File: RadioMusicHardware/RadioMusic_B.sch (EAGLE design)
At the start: 32 parts, among them IC4 TL074, U1 TEENSY_3.1_TW

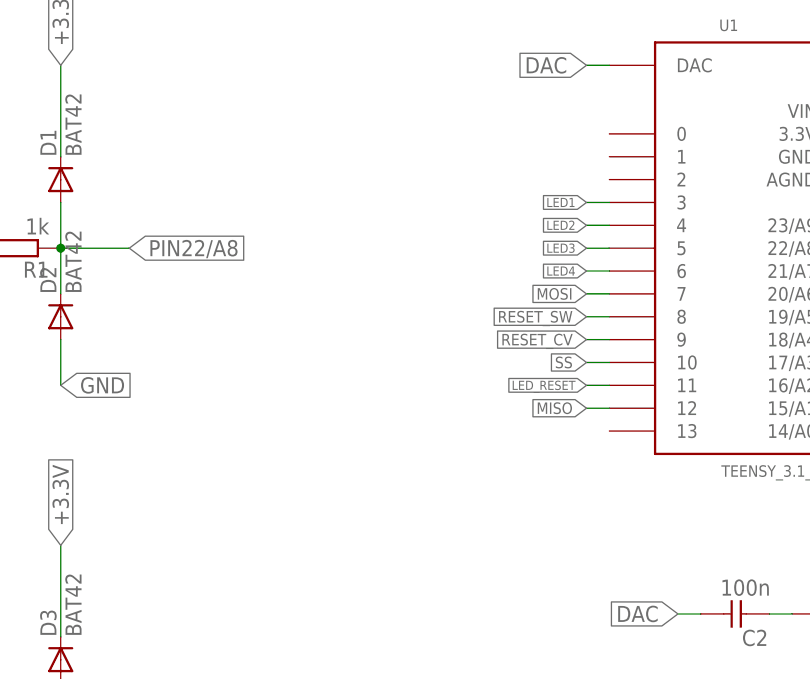
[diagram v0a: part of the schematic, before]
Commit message: Layout experiments - back board output not completed
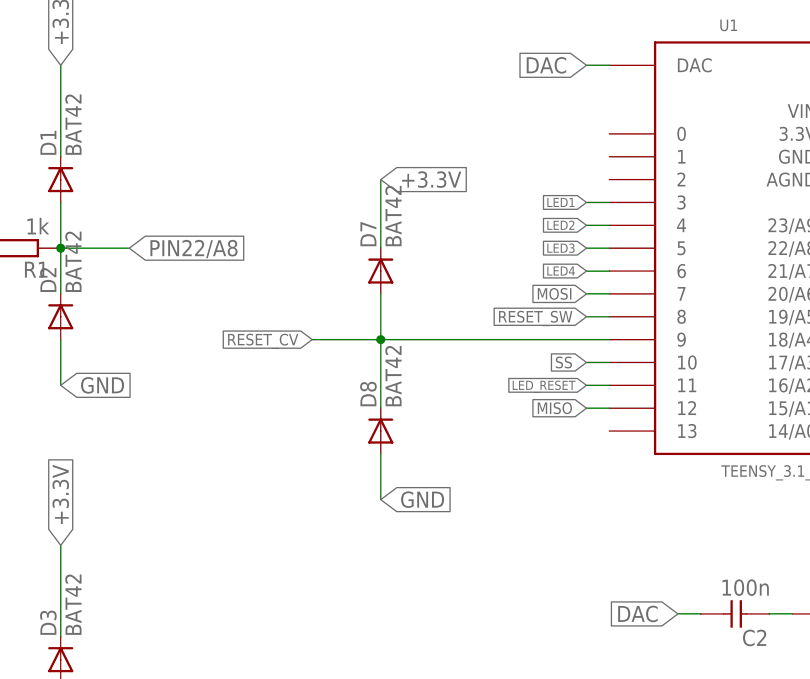
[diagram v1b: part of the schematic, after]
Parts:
- added D7, D8: BAT42, MusicThingModular:SMALL_DIODEDO35-7
- D1, D2, D3, D4: device diode:BAT81 -> MusicThingModular:SMALL_DIODEDO35-7
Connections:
- net +3.3V: now also D7.C
- net GND: now also D8.A
- net RESET_CV: now also D7.A, D8.C
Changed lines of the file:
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@@
 <part name="SUPPLY2" library="supply2" deviceset="GND" device=""/>
 <part name="U1" library="TomW" deviceset="TEENSY_3.1_TW" device=""/>
-<part name="D1" library="diode" deviceset="BAT81" device="" value="BAT42"/>
-<part name="D2" library="diode" deviceset="BAT81" device="" value="BAT42"/>
+<part name="D1" library="MusicThingModular" deviceset="SMALL_DIODE" device="DO35-7" value="BAT42"/>
+<part name="D2" library="MusicThingModular" deviceset="SMALL_DIODE" device="DO35-7" value="BAT42"/>
 <part name="R4" library="MusicThingModular" deviceset="RESISTOR" device="7MM" value="8.2k"/>
 <part name="R3" library="MusicThingModular" deviceset="RESISTOR" device="7MM" value="8.2k"/>
@@
 <part name="C2" library="TomW" deviceset="C-EU" device="050-025X075" value="100n"/>
 <part name="R1" library="TomW" deviceset="R-EU_" device="STANDARD_RESISTOR" value="1k"/>
-<part name="D3" library="diode" deviceset="BAT81" device="" value="BAT42"/>
-<part name="D4" library="diode" deviceset="BAT81" device="" value="BAT42"/>
+<part name="D3" library="MusicThingModular" deviceset="SMALL_DIODE" device="DO35-7" value="BAT42"/>
+<part name="D4" library="MusicThingModular" deviceset="SMALL_DIODE" device="DO35-7" value="BAT42"/>
 <part name="R2" library="TomW" deviceset="R-EU_" device="STANDARD_RESISTOR" value="1k"/>
 <part name="L1" library="inductors" deviceset="BL0" device="1RN1A"/>
@@
 <part name="IC1" library="v-reg" deviceset="78LXX" device=""/>
 <part name="R6" library="MusicThingModular" deviceset="RESISTOR" device="7MM" value="100k"/>
+<part name="D7" library="MusicThingModular" deviceset="SMALL_DIODE" device="DO35-7" value="BAT42"/>
+<part name="D8" library="MusicThingModular" deviceset="SMALL_DIODE" device="DO35-7" value="BAT42"/>
 </parts>
 <sheets>
@@
 <instance part="IC4" gate="D" x="182.88" y="71.12"/>
 <instance part="IC4" gate="A" x="231.14" y="68.58"/>
-<instance part="D1" gate="1" x="40.64" y="121.92" rot="R90"/>
-<instance part="D2" gate="1" x="40.64" y="106.68" rot="R90"/>
+<instance part="D1" gate="G$1" x="40.64" y="121.92" rot="R90"/>
+<instance part="D2" gate="G$1" x="40.64" y="106.68" rot="R90"/>
 <instance part="R4" gate="G$1" x="149.86" y="73.66"/>
 <instance part="R3" gate="G$1" x="127" y="73.66" rot="R180"/>
@@
 <instance part="R1" gate="G$1" x="35.56" y="114.3" rot="R180"/>
 <instance part="IC4" gate="C" x="17.78" y="60.96"/>
-<instance part="D3" gate="1" x="40.64" y="68.58" rot="R90"/>
-<instance part="D4" gate="1" x="40.64" y="53.34" rot="R90"/>
+<instance part="D3" gate="G$1" x="40.64" y="68.58" rot="R90"/>
+<instance part="D4" gate="G$1" x="40.64" y="53.34" rot="R90"/>
 <instance part="R2" gate="G$1" x="35.56" y="60.96" rot="R180"/>
 <instance part="L1" gate="G$1" x="149.86" y="33.02" rot="R180"/>
@@
 <instance part="IC1" gate="1" x="91.44" y="38.1"/>
 <instance part="R6" gate="G$1" x="162.56" y="55.88" rot="R90"/>
+<instance part="D7" gate="G$1" x="76.2" y="111.76" rot="R90"/>
+<instance part="D8" gate="G$1" x="76.2" y="93.98" rot="R90"/>
 </instances>
 <busses>
@@
 </segment>
 <segment>
-<pinref part="D2" gate="1" pin="A"/>
+<pinref part="D2" gate="G$1" pin="A"/>
 <wire x1="40.64" y1="99.06" x2="40.64" y2="104.14" width="0.1524" layer="91"/>
 <label x="40.64" y="99.06" size="1.778" layer="95" xref="yes"/>
 </segment>
 <segment>
-<pinref part="D4" gate="1" pin="A"/>
+<pinref part="D4" gate="G$1" pin="A"/>
 <wire x1="40.64" y1="45.72" x2="40.64" y2="50.8" width="0.1524" layer="91"/>
 <label x="40.64" y="45.72" size="1.778" layer="95" xref="yes"/>
+</segment>
+<segment>
+<pinref part="D8" gate="G$1" pin="A"/>
+<wire x1="76.2" y1="91.44" x2="76.2" y2="86.36" width="0.1524" layer="91"/>
+<label x="76.2" y="86.36" size="1.778" layer="95" xref="yes"/>
 </segment>
 </net>
@@
 </segment>
 <segment>
-<pinref part="D1" gate="1" pin="C"/>
+<pinref part="D1" gate="G$1" pin="C"/>
 <wire x1="40.64" y1="134.62" x2="40.64" y2="124.46" width="0.1524" layer="91"/>
 <label x="40.64" y="134.62" size="1.778" layer="95" rot="R90" xref="yes"/>
 </segment>
 <segment>
-<pinref part="D3" gate="1" pin="C"/>
+<pinref part="D3" gate="G$1" pin="C"/>
 <wire x1="40.64" y1="81.28" x2="40.64" y2="71.12" width="0.1524" layer="91"/>
 <label x="40.64" y="81.28" size="1.778" layer="95" rot="R90" xref="yes"/>
@@
 <label x="195.58" y="109.22" size="1.016" layer="95" rot="R180" xref="yes"/>
 </segment>
+<segment>
+<pinref part="D7" gate="G$1" pin="C"/>
+<wire x1="76.2" y1="114.3" x2="76.2" y2="121.92" width="0.1524" layer="91"/>
+<label x="76.2" y="121.92" size="1.778" layer="95" xref="yes"/>
+</segment>
 </net>
 <net name="CHANNEL_CV" class="0">
@@
 </segment>
 <segment>
-<pinref part="D1" gate="1" pin="A"/>
+<pinref part="D1" gate="G$1" pin="A"/>
 <wire x1="40.64" y1="119.38" x2="40.64" y2="114.3" width="0.1524" layer="91"/>
-<pinref part="D2" gate="1" pin="C"/>
+<pinref part="D2" gate="G$1" pin="C"/>
 <wire x1="40.64" y1="109.22" x2="40.64" y2="114.3" width="0.1524" layer="91"/>
 <junction x="40.64" y="114.3"/>
@@
 <net name="PIN20/A6" class="0">
 <segment>
-<pinref part="D3" gate="1" pin="A"/>
+<pinref part="D3" gate="G$1" pin="A"/>
 <wire x1="40.64" y1="66.04" x2="40.64" y2="60.96" width="0.1524" layer="91"/>
-<pinref part="D4" gate="1" pin="C"/>
+<pinref part="D4" gate="G$1" pin="C"/>
 <wire x1="40.64" y1="55.88" x2="40.64" y2="60.96" width="0.1524" layer="91"/>
 <junction x="40.64" y="60.96"/>
@@
 <segment>
 <pinref part="U1" gate="G$1" pin="9"/>
-<wire x1="99.06" y1="104.14" x2="101.6" y2="104.14" width="0.1524" layer="91"/>
-<label x="99.06" y="104.14" size="1.27" layer="95" rot="R180" xref="yes"/>
-</segment>
-<segment>
+<wire x1="68.58" y1="104.14" x2="76.2" y2="104.14" width="0.1524" layer="91"/>
+<label x="68.58" y="104.14" size="1.27" layer="95" rot="R180" xref="yes"/>
+<pinref part="D7" gate="G$1" pin="A"/>
+<wire x1="76.2" y1="104.14" x2="101.6" y2="104.14" width="0.1524" layer="91"/>
+<wire x1="76.2" y1="109.22" x2="76.2" y2="104.14" width="0.1524" layer="91"/>
+<junction x="76.2" y="104.14"/>
+<pinref part="D8" gate="G$1" pin="C"/>
+<wire x1="76.2" y1="96.52" x2="76.2" y2="104.14" width="0.1524" layer="91"/>
+</segment>
+<segment>

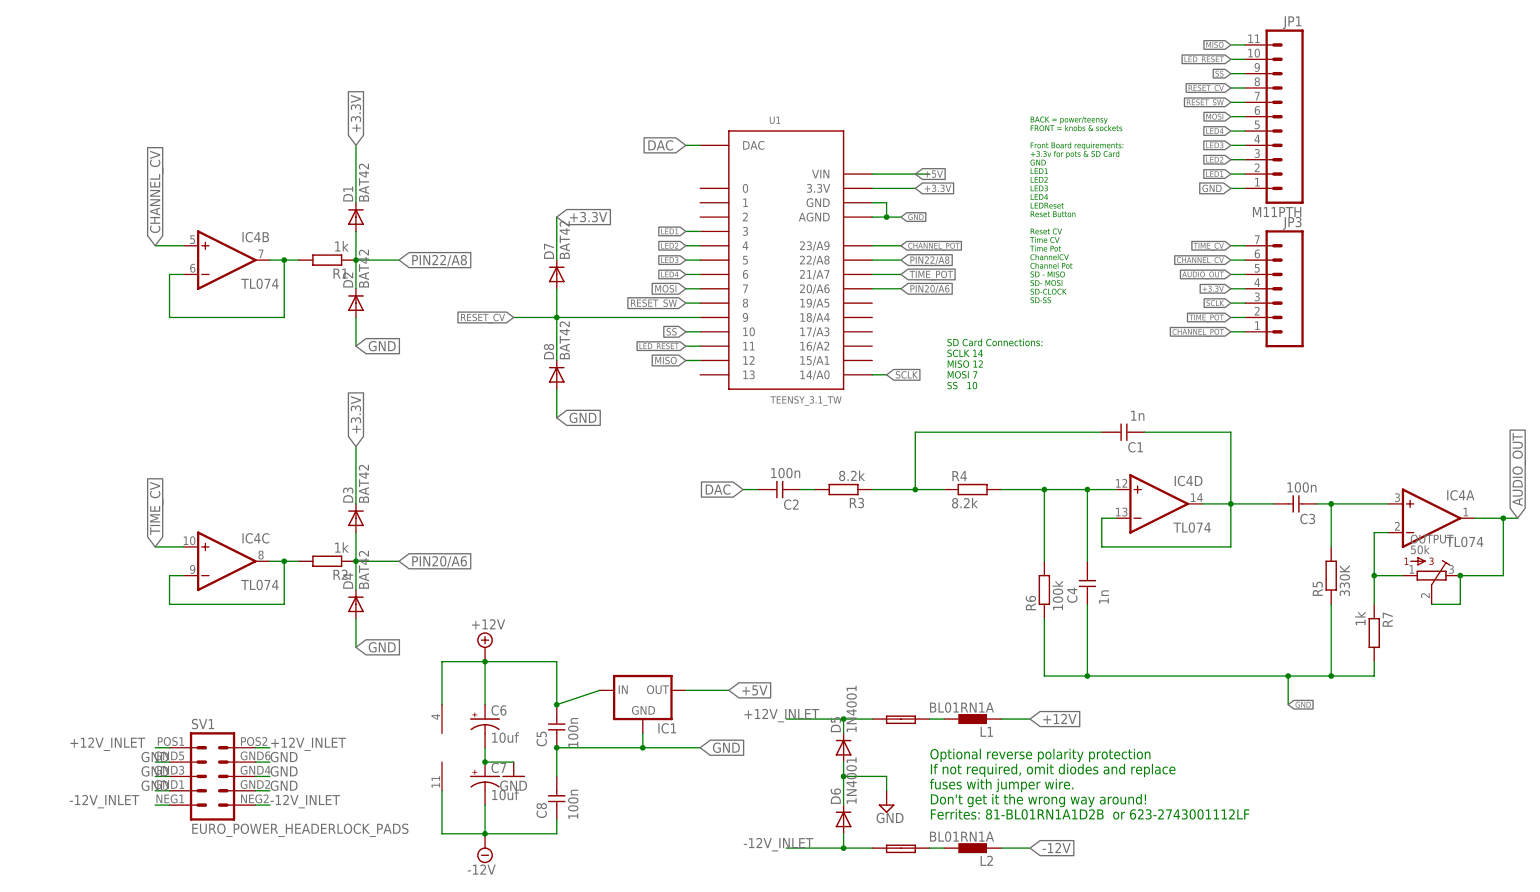
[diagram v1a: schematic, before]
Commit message: schematic complete, rear not laid out
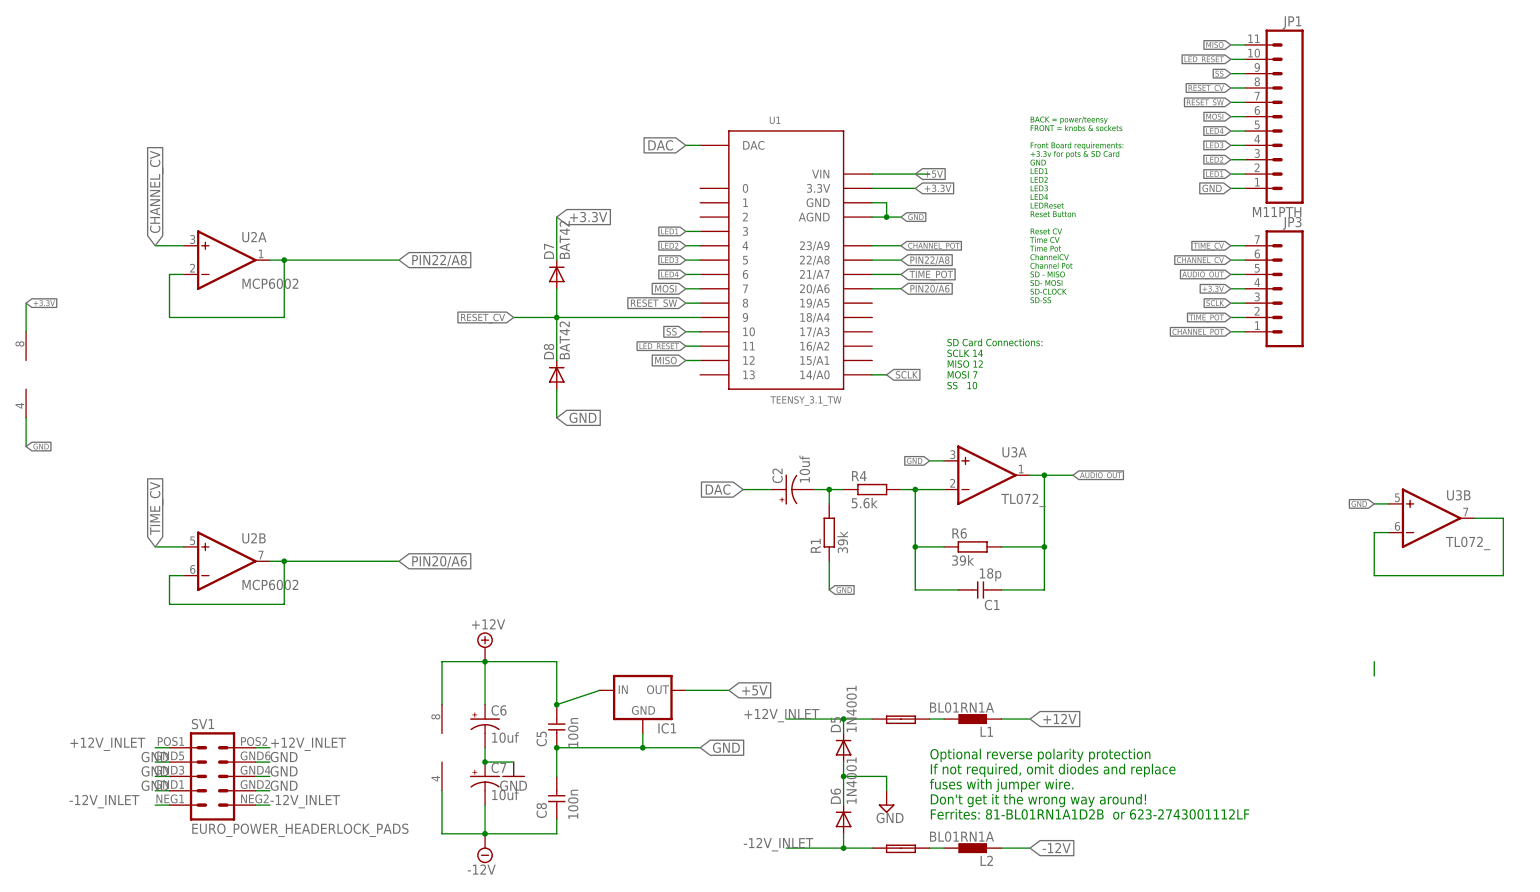
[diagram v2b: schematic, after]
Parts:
- removed C3: 100n, TomW:C-EU050-025X075
- removed C4: 1n, TomW:C-EU050-024X044
- removed D1, D2, D3, D4: BAT42, MusicThingModular:SMALL_DIODEDO35-7
- removed IC4: TL074, linear:TL074P
- removed OUTPUT: 50k, bourns:3362P
- removed R2: 1k, TomW:R-EU_STANDARD_RESISTOR
- removed R3: 8.2k, MusicThingModular:RESISTOR7MM
- removed R5: 330K, MusicThingModular:RESISTOR7MM
- removed R7: 1k, MusicThingModular:RESISTOR7MM
- added U2: MCP6002, MusicThingModular:TL072_
- added U3: TL072_, MusicThingModular:TL072_
- C1: value 1n -> 18p
- C2: value 100n -> 10uf; device TomW:C-EU050-025X075 -> SparkFun-Passives:CAP_POLPTH2
- R1: value 1k -> 39k; device TomW:R-EU_STANDARD_RESISTOR -> MusicThingModular:RESISTOR7MM
- R4: value 8.2k -> 5.6k
- R6: value 100k -> 39k
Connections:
- removed net N$10: C2.2, R3.2
- removed net N$2: C4.1, IC4D.+IN, R4.2, R6.2
- removed net N$3: IC4B.-IN, IC4B.OUT, R1.2
- removed net N$5: C1.2, C3.1, IC4D.-IN, IC4D.OUT
- removed net N$6: C3.2, IC4A.+IN, R5.2
- net +12V: now also U3P.V+; no longer IC4P.V+
- net +3.3V: now also U2P.V+; no longer D1.C, D3.C
- net -12V: now also U3P.V-; no longer IC4P.V-
- net AUDIO_OUT: now also C1.2, R6.2, U3A.OUT; no longer IC4A.OUT, OUTPUT.2, OUTPUT.3
- net CHANNEL_CV: now also U2A.+IN; no longer IC4B.+IN
- net DAC: now also C2.+; no longer C2.1
- net GND: now also U2P.V-, U3A.+IN, U3B.+IN; no longer C4.2, D2.A, D4.A, R5.1, R6.1, R7.2
- net N$1: now also C2.-, R1.2, R4.1; no longer IC4C.-IN, IC4C.OUT, R2.2
- net N$4: now also R4.2, R6.1, U3A.-IN; no longer R3.1, R4.1
- net N$7: now also U3B.-IN, U3B.OUT; no longer IC4A.-IN, OUTPUT.1, R7.1
- net PIN20/A6: now also U2B.-IN, U2B.OUT; no longer D3.A, D4.C, R2.1
- net PIN22/A8: now also U2A.-IN, U2A.OUT; no longer D1.A, D2.C, R1.1
- net TIME_CV: now also U2B.+IN; no longer IC4C.+IN
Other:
- moved on the sheet: C1, R1, R4, R6
